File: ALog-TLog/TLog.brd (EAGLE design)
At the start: 124.1 x 45.3 mm, 101 parts, among them IC1 ATMEGA644M, J6 5.5x2.1mm Barrel, Q5 MOSFET_PCH-IRLML2244, Q6 MOSFET_PCH-IRLML2244, Q7 MOSFET_PCH-IRLML2244, Q8 MOSFET-NCH-BSS138, Q9 MOSFET-NCH-BSS138, U2 FT231X-Q, U3 915MHz, U4 SX1509, X2 87832-14

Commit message: Presumptive Final gerbers for TLog Mrk 1.1
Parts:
- ISP2: device adafruit:AVRISP -> bschulz:AVRISP
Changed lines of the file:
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@@
 <?xml version="1.0" encoding="utf-8"?>
 <!DOCTYPE eagle SYSTEM "eagle.dtd">
-<eagle version="8.3.2">
+<eagle version="8.5.1">
 <drawing>
 <settings>
@@
 <layer number="22" name="bPlace" color="7" fill="1" visible="yes" active="yes"/>
 <layer number="23" name="tOrigins" color="15" fill="1" visible="yes" active="yes"/>
-<layer number="24" name="bOrigins" color="15" fill="1" visible="yes" active="yes"/>
-<layer number="25" name="tNames" color="7" fill="1" visible="yes" active="yes"/>
-<layer number="26" name="bNames" color="7" fill="1" visible="yes" active="yes"/>
-<layer number="27" name="tValues" color="7" fill="1" visible="yes" active="yes"/>
-<layer number="28" name="bValues" color="7" fill="1" visible="yes" active="yes"/>
+<layer number="24" name="bOrigins" color="15" fill="1" visible="no" active="yes"/>
+<layer number="25" name="tNames" color="7" fill="1" visible="no" active="yes"/>
+<layer number="26" name="bNames" color="7" fill="1" visible="no" active="yes"/>
+<layer number="27" name="tValues" color="7" fill="1" visible="no" active="yes"/>
+<layer number="28" name="bValues" color="7" fill="1" visible="no" active="yes"/>
 <layer number="29" name="tStop" color="7" fill="3" visible="no" active="yes"/>
 <layer number="30" name="bStop" color="7" fill="6" visible="no" active="yes"/>
@@
 <layer number="37" name="tTest" color="7" fill="1" visible="no" active="yes"/>
 <layer number="38" name="bTest" color="7" fill="1" visible="no" active="yes"/>
-<layer number="39" name="tKeepout" color="4" fill="11" visible="yes" active="yes"/>
-<layer number="40" name="bKeepout" color="1" fill="11" visible="yes" active="yes"/>
-<layer number="41" name="tRestrict" color="4" fill="10" visible="yes" active="yes"/>
-<layer number="42" name="bRestrict" color="1" fill="10" visible="yes" active="yes"/>
+<layer number="39" name="tKeepout" color="4" fill="11" visible="no" active="yes"/>
+<layer number="40" name="bKeepout" color="1" fill="11" visible="no" active="yes"/>
+<layer number="41" name="tRestrict" color="4" fill="10" visible="no" active="yes"/>
+<layer number="42" name="bRestrict" color="1" fill="10" visible="no" active="yes"/>
 <layer number="43" name="vRestrict" color="2" fill="10" visible="no" active="yes"/>
 <layer number="44" name="Drills" color="7" fill="1" visible="yes" active="yes"/>
@@
 <wire x1="0.127" y1="45.36525" x2="0.127" y2="0.09525" width="0.254" layer="20"/>
 <rectangle x1="28.477" y1="25.804" x2="28.757" y2="26.254" layer="29"/>
-<text x="4.699" y="39.497" size="1.778" layer="51" font="vector" ratio="10" rot="SR180">RST</text>
-<text x="4.953" y="7.493" size="1.778" layer="51" font="vector" ratio="10" rot="SR180">LOG</text>
+<text x="5.08" y="39.497" size="1.778" layer="51" font="vector" ratio="10" rot="SR180">RST</text>
+<text x="5.08" y="7.747" size="1.778" layer="51" font="vector" ratio="10" rot="SR180">LOG</text>
 <text x="15.60625625" y="8.755959375" size="1.27" layer="51" font="vector" ratio="10" rot="SR180">GND</text>
 <text x="18.377803125" y="9.614803125" size="1.27" layer="51" font="vector" ratio="10" rot="SR225">A0</text>
@@
 parntnership with
 Northern Widget LLC</text>
-<text x="44.7664" y="11.284" size="0.6096" layer="22" rot="MR0">TM</text>
+<text x="43.736" y="10.994" size="0.8128" layer="22" font="vector" ratio="20" rot="MR0" align="bottom-right">TM</text>
 </plain>
 <attributes>
@@
 <param name="dpMaxLengthDifference" value="10mm"/>
 <param name="dpGapFactor" value="2.5"/>
-<param name="checkGrid" value="0"/>
 <param name="checkAngle" value="0"/>
 <param name="checkFont" value="1"/>
 <param name="checkRestrict" value="1"/>
+<param name="checkStop" value="0"/>
+<param name="checkValues" value="0"/>
 <param name="useDiameter" value="13"/>
 <param name="maxErrors" value="50"/>
@@
 <attribute name="MPN" value="MF-NSMF020-2" x="79.8195" y="22.352" size="1.778" layer="27" rot="R180" display="off"/>
 </element>
-<element name="ISP2" library="adafruit" library_urn="urn:adsk.eagle:library:420" package="AVRISP" value="AVRISP-6" x="21.209" y="37.084" smashed="yes" rot="R90">
+<element name="ISP2" library="bschulz" package="AVRISP" value="AVRISP-6" x="21.209" y="37.084" smashed="yes" rot="R90">
 <attribute name="DIGIKEY" value="609-3234-ND" x="21.209" y="37.084" size="1.778" layer="27" rot="R90" display="off"/>
 <attribute name="MF" value="Amphenol" x="21.209" y="37.084" size="1.778" layer="27" rot="R90" display="off"/>

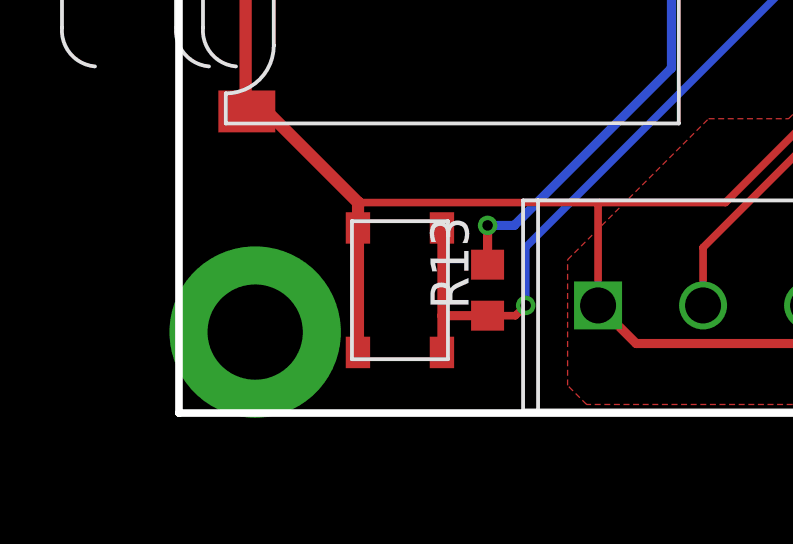
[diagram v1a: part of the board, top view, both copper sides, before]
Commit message: Final Gerbers for TLog Mrk 1.1
Gerbers_9.zip contains the gerber files used in the TLog 1.1 production run (order placed on 1/5/2017)
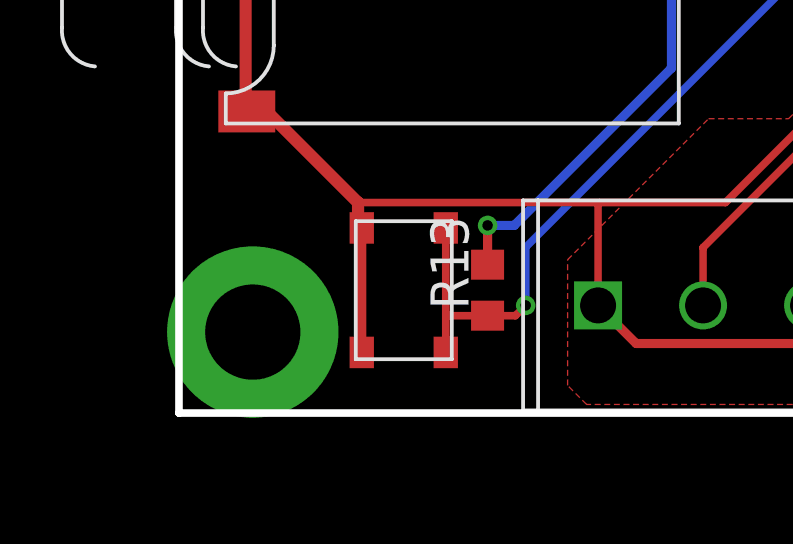
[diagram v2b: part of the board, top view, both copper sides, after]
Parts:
- moved U$5 0.13 mm to (7.62, 4.19)
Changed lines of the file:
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@@
 <?xml version="1.0" encoding="utf-8"?>
 <!DOCTYPE eagle SYSTEM "eagle.dtd">
-<eagle version="8.5.1">
+<eagle version="8.3.0">
 <drawing>
 <settings>
@@
 <setting verticaltext="up"/>
 </settings>
-<grid distance="0.127" unitdist="mm" unit="mil" style="lines" multiple="1" display="no" altdistance="0.0635" altunitdist="mm" altunit="mil"/>
+<grid distance="0.127" unitdist="mm" unit="mm" style="lines" multiple="1" display="no" altdistance="0.0635" altunitdist="mm" altunit="mm"/>
 <layers>
 <layer number="1" name="Top" color="4" fill="1" visible="yes" active="yes"/>
@@
 <layer number="22" name="bPlace" color="7" fill="1" visible="yes" active="yes"/>
 <layer number="23" name="tOrigins" color="15" fill="1" visible="yes" active="yes"/>
-<layer number="24" name="bOrigins" color="15" fill="1" visible="no" active="yes"/>
-<layer number="25" name="tNames" color="7" fill="1" visible="no" active="yes"/>
-<layer number="26" name="bNames" color="7" fill="1" visible="no" active="yes"/>
-<layer number="27" name="tValues" color="7" fill="1" visible="no" active="yes"/>
-<layer number="28" name="bValues" color="7" fill="1" visible="no" active="yes"/>
+<layer number="24" name="bOrigins" color="15" fill="1" visible="yes" active="yes"/>
+<layer number="25" name="tNames" color="7" fill="1" visible="yes" active="yes"/>
+<layer number="26" name="bNames" color="7" fill="1" visible="yes" active="yes"/>
+<layer number="27" name="tValues" color="7" fill="1" visible="yes" active="yes"/>
+<layer number="28" name="bValues" color="7" fill="1" visible="yes" active="yes"/>
 <layer number="29" name="tStop" color="7" fill="3" visible="no" active="yes"/>
 <layer number="30" name="bStop" color="7" fill="6" visible="no" active="yes"/>
@@
 <layer number="37" name="tTest" color="7" fill="1" visible="no" active="yes"/>
 <layer number="38" name="bTest" color="7" fill="1" visible="no" active="yes"/>
-<layer number="39" name="tKeepout" color="4" fill="11" visible="no" active="yes"/>
-<layer number="40" name="bKeepout" color="1" fill="11" visible="no" active="yes"/>
-<layer number="41" name="tRestrict" color="4" fill="10" visible="no" active="yes"/>
-<layer number="42" name="bRestrict" color="1" fill="10" visible="no" active="yes"/>
+<layer number="39" name="tKeepout" color="4" fill="11" visible="yes" active="yes"/>
+<layer number="40" name="bKeepout" color="1" fill="11" visible="yes" active="yes"/>
+<layer number="41" name="tRestrict" color="4" fill="10" visible="yes" active="yes"/>
+<layer number="42" name="bRestrict" color="1" fill="10" visible="yes" active="yes"/>
 <layer number="43" name="vRestrict" color="2" fill="10" visible="no" active="yes"/>
 <layer number="44" name="Drills" color="7" fill="1" visible="yes" active="yes"/>
@@
 <text x="54.527903125" y="9.6892" size="1.27" layer="51" font="vector" ratio="10" rot="SR225">A5</text>
 <text x="58.382803125" y="10.72060625" size="1.27" layer="51" font="vector" ratio="10" rot="SR225">INT1</text>
-<text x="62.252453125" y="9.8245625" size="1.27" layer="51" font="vector" ratio="10" rot="SR225">5V</text>
+<text x="61.490453125" y="10.2055625" size="1.27" layer="51" font="vector" ratio="10" rot="SR225">5V</text>
 <text x="65.621803125" y="10.29470625" size="1.27" layer="51" font="vector" ratio="10" rot="SR225">3V3</text>
 <text x="69.080296875" y="10.376803125" size="1.27" layer="51" font="vector" ratio="10" rot="SR225">GND</text>
@@
 <text x="21.87575" y="33.49625" size="1.27" layer="51" font="vector" ratio="10" rot="SR180">ISP</text>
 <text x="115.22075" y="44.7675" size="1.27" layer="51" font="vector" ratio="10" rot="SR180">VIN</text>
-<text x="32.639" y="44.831" size="1.27" layer="51" font="vector" ratio="10" rot="SR180">A6</text>
-<text x="36.576" y="44.831" size="1.27" layer="51" font="vector" ratio="10" rot="SR180">A7</text>
-<text x="39.878" y="44.831" size="1.27" layer="51" font="vector" ratio="10" rot="SR180">A8</text>
-<text x="43.40225" y="44.831" size="1.27" layer="51" font="vector" ratio="10" rot="SR180">A9</text>
-<text x="47.625" y="44.831" size="1.27" layer="51" font="vector" ratio="10" rot="SR180">A10</text>
+<text x="32.512" y="44.831" size="1.27" layer="51" font="vector" ratio="10" rot="SR180">A6</text>
+<text x="35.814" y="44.831" size="1.27" layer="51" font="vector" ratio="10" rot="SR180">A7</text>
+<text x="39.243" y="44.831" size="1.27" layer="51" font="vector" ratio="10" rot="SR180">A8</text>
+<text x="42.76725" y="44.831" size="1.27" layer="51" font="vector" ratio="10" rot="SR180">A9</text>
+<text x="47.244" y="44.831" size="1.27" layer="51" font="vector" ratio="10" rot="SR180">A10</text>
 <text x="51.562" y="44.831" size="1.27" layer="51" font="vector" ratio="10" rot="SR180">A11</text>
 <text x="54.61" y="44.831" size="1.27" layer="51" font="vector" ratio="10" rot="SR180">D0</text>
@@
 <param name="dpMaxLengthDifference" value="10mm"/>
 <param name="dpGapFactor" value="2.5"/>
+<param name="checkGrid" value="0"/>
 <param name="checkAngle" value="0"/>
 <param name="checkFont" value="1"/>
 <param name="checkRestrict" value="1"/>
-<param name="checkStop" value="0"/>
-<param name="checkValues" value="0"/>
 <param name="useDiameter" value="13"/>
 <param name="maxErrors" value="50"/>
@@
 <attribute name="VALUE_PART" value="330" x="48.641" y="33.02" size="1.778" layer="27" rot="R180" display="off"/>
 </element>
-<element name="U$5" library="bschulz" package="SWITCH_4.2X3.2" value="BUTTON4.2X3.2" x="7.493" y="4.191" smashed="yes" rot="R90"/>
+<element name="U$5" library="bschulz" package="SWITCH_4.2X3.2" value="BUTTON4.2X3.2" x="7.62" y="4.191" smashed="yes" rot="R90"/>
 <element name="R13" library="bschulz" package="R0603" value="10k" x="10.414" y="4.191" smashed="yes" rot="R90">
 <attribute name="DIGIKEY" value="311-10.0KHRCT-ND" x="10.414" y="4.191" size="1.778" layer="27" rot="R90" display="off"/>
@@
 <contactref element="U$5" pad="2"/>
 <wire x1="13.1445" y1="43.59275" x2="12.99125" y2="43.746" width="0.4064" layer="1"/>
-<wire x1="6.093" y1="6.090375" x2="6.093" y2="6.266" width="0.4064" layer="1"/>
-<wire x1="6.093" y1="6.090375" x2="6.093" y2="2.116" width="0.4064" layer="1"/>
+<wire x1="6.093" y1="6.090375" x2="6.22" y2="6.266" width="0.4064" layer="1"/>
 <wire x1="9.035" y1="43.746" x2="9.02" y2="43.731" width="0.4064" layer="1"/>
 <wire x1="12.99125" y1="43.746" x2="9.035" y2="43.746" width="0.4064" layer="1"/>
@@
 <wire x1="71.374" y1="9.525" x2="71.374" y2="10.834" width="0.3048" layer="1"/>
 <wire x1="75.3745" y1="9.525" x2="71.374" y2="9.525" width="0.3048" layer="1"/>
+<wire x1="6.22" y1="6.266" x2="6.22" y2="2.116" width="0.3048" layer="1"/>
+<wire x1="101.292" y1="33.21" x2="101.692" y2="33.21" width="0" layer="19" extent="1-1"/>
+<wire x1="100.892" y1="33.21" x2="101.292" y2="33.21" width="0" layer="19" extent="1-1"/>
+<wire x1="100.492" y1="33.21" x2="100.892" y2="33.21" width="0" layer="19" extent="1-1"/>
+<wire x1="101.092" y1="32.385" x2="101.292" y2="33.21" width="0" layer="19" extent="1-1"/>
+<wire x1="101.092" y1="31.75" x2="101.092" y2="32.35" width="0" layer="19" extent="1-1"/>
+<wire x1="101.092" y1="31.15" x2="101.092" y2="31.75" width="0" layer="19" extent="1-1"/>
+<wire x1="96.818975" y1="35.184975" x2="96.774" y2="35.7806" width="0" layer="19" extent="1-1"/>
+<wire x1="95.367" y1="22.094" x2="94.5642" y2="22.9108" width="0" layer="19" extent="1-16"/>
 <wire x1="121.6025" y1="7.874" x2="121.6025" y2="7.874" width="0" layer="19" extent="1-16"/>
 <wire x1="121.6025" y1="2.794" x2="121.6025" y2="2.794" width="0" layer="19" extent="1-16"/>
+<wire x1="101.561" y1="34.798" x2="102.46329375" y2="35.7806" width="0" layer="19" extent="1-1"/>
+<wire x1="30.861" y1="35.336" x2="32.4162" y2="34.5274" width="0" layer="19" extent="1-1"/>
+<wire x1="106.299" y1="32.446" x2="104.394" y2="32.446" width="0" layer="19" extent="1-1"/>
+<wire x1="86.94345" y1="25.4635" x2="87.767" y2="22.094" width="0" layer="19" extent="1-1"/>
 </signal>
 <signal name="RST">
@@
 </signal>
 <signal name="N$12">
-<via x="2.667" y="2.794" extent="1-16" drill="3.175" shape="octagon"/>
+<via x="2.587625" y="2.794" extent="1-16" drill="3.175" shape="octagon"/>
 </signal>
 <signal name="N$17">
@@
 <contactref element="U$5" pad="3"/>
 <contactref element="R13" pad="1"/>
-<wire x1="8.893" y1="3.341" x2="8.893" y2="6.266" width="0.3048" layer="1"/>
-<wire x1="8.893" y1="3.341" x2="8.893" y2="2.116" width="0.3048" layer="1"/>
-<wire x1="8.893" y1="3.341" x2="10.414" y2="3.341" width="0.3048" layer="1"/>
-<wire x1="10.414" y1="3.341" x2="11.342" y2="3.341" width="0.254" layer="1"/>
+<wire x1="11.342" y1="3.341" x2="10.414" y2="3.341" width="0.254" layer="1"/>
 <wire x1="11.342" y1="3.341" x2="11.684" y2="3.683" width="0.254" layer="1"/>
 <via x="11.684" y="3.683" extent="1-16" drill="0.35" shape="octagon"/>
@@
 <wire x1="54.737" y1="22.252325" x2="56.31395625" y2="22.252325" width="0.254" layer="1"/>
 <wire x1="56.31395625" y1="22.252325" x2="57.15" y2="21.41628125" width="0.254" layer="1"/>
+<wire x1="9.02" y1="3.314171875" x2="9.02" y2="6.266" width="0.254" layer="1"/>
+<wire x1="9.02" y1="3.314171875" x2="9.02" y2="2.116" width="0.254" layer="1"/>
+<wire x1="10.414" y1="3.341" x2="9.046828125" y2="3.341" width="0.254" layer="1"/>
+<wire x1="9.046828125" y1="3.341" x2="9.02" y2="3.314171875" width="0.254" layer="1"/>
 </signal>
 <signal name="3V3">

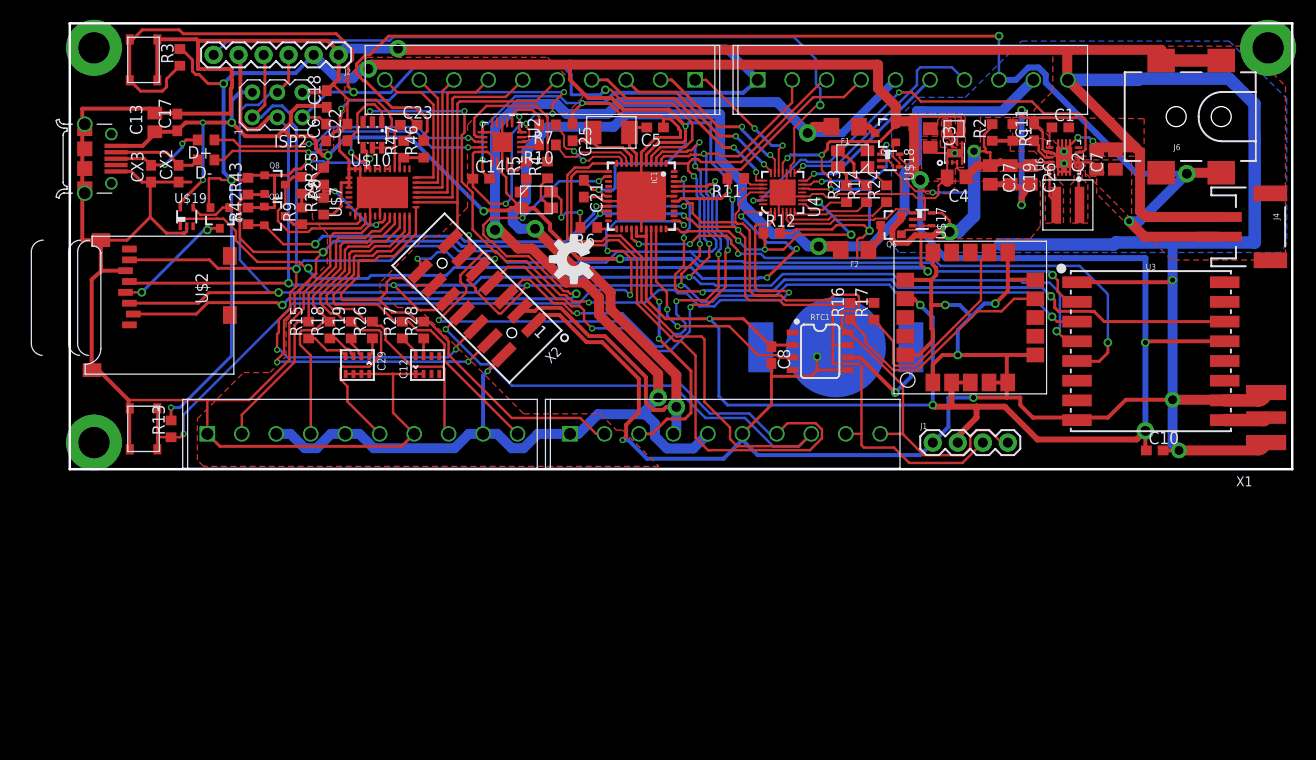
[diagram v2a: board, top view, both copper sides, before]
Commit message: Issue Fix
Patial fix of issues: #12, #9, #8 (fixed in schematic, but not fully routed)
Full fix of issues: #10, #7
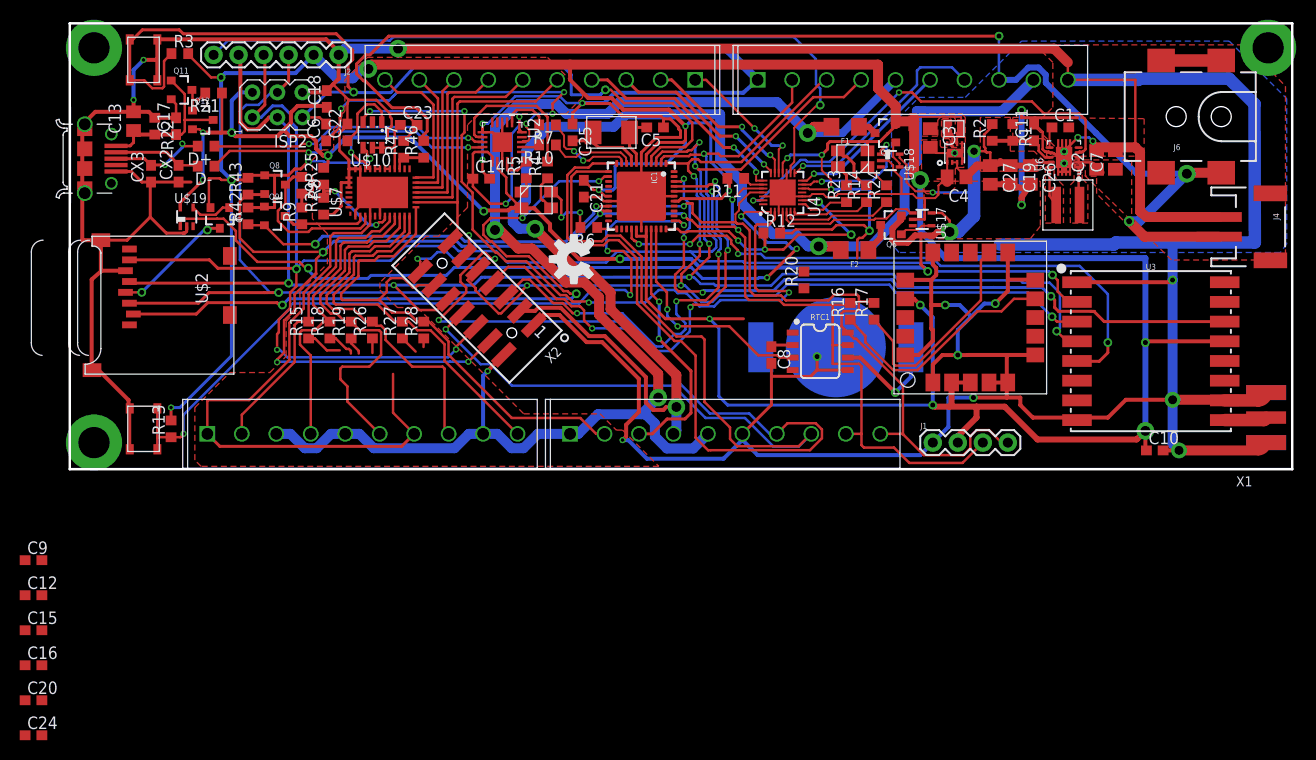
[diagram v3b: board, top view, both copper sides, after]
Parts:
- removed C29: 10nF, rc-master-smd:CECJ-1206
- added C15, C16, C20, C24, C9: (no value), bschulz_passives:C0603
- added Q11: MOSFET-NCH-BSS138, bschulz:SOT23-3
- added Q12: MOSFET_PCH-IRLML2244, bschulz:SOT23-3
- added R20: 180k, bschulz_passives:R0603
- added R21, R22: 10k, rcl:R0603
- C12: value 10nF -> (none); device rc-master-smd:CECJ-1206 -> bschulz_passives:C0603
- moved C12 46.3 mm to (-3.56, -12.7)
- moved C13 2.16 mm to (6.60, 35.4)
- moved D+ 0.63 mm to (14.0, 32.9)
- moved D- 0.63 mm to (14.0, 30.9)
- moved C17 0.40 mm to (10.9, 34.9)
- moved R3 0.38 mm to (11.3, 42.3), turned to 0 degrees
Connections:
- removed net N$17: C12.B2, R28.1
- removed net N$19: C29.B1, R19.1
- removed net N$24: C29.A1, R26.1
- removed net N$44: C29.D1, R15.1
- removed net N$45: C29.C1, R18.1
- removed net N$48: C12.A2, R27.1
- new net 5V_EXT: R25.2
- new net N$34: Q11.3, Q12.1, R21.2
- new net VUSB: C13.1, C17.1, MICRO_USB.1, Q11.1, Q12.3, R22.2
- net 3V3: now also R20.2; no longer C8.1, RTC1.2
- net 5V: now also Q12.2, R21.1; no longer C13.1, C17.1, MICRO_USB.1, R25.2
- net ADC0: now also C9.1
- net ADC1: now also C12.1
- net ADC2: now also C15.1
- net ADC3: now also C16.1
- net ADC4: now also C20.1
- net ADC5: now also C24.1
- net EXT_3.3V: now also C8.1, RTC1.2
- net GND: now also C12.2, C15.2, C16.2, C20.2, C24.2, C9.2, Q11.2, R15.1, R18.1, R19.1, R22.1, R26.1, R27.1, R28.1; no longer C12.A1, C12.B1, C29.A2, C29.B2, C29.C2, C29.D2
- net REF_CTRL: now also R20.1
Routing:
- net GND: track 841.5 -> 822.7 mm, vias 18 -> 20
- net VUSB: track 0.00 -> 17.7 mm
- net 3V3: track 426.5 -> 418.8 mm
- net 5V: track 185.7 -> 178.4 mm
- net N$44: track 4.50 -> 0.00 mm
- net N$34: track 0.00 -> 3.70 mm
- net N$45: track 3.30 -> 0.00 mm
- net N$48: track 2.36 -> 0.00 mm
- net N$19: track 2.23 -> 0.00 mm
- net EXT_3.3V: track 147.6 -> 149.8 mm
- net N$24: track 1.94 -> 0.00 mm
- net N$17: track 1.81 -> 0.00 mm
- net N$38: track 29.2 -> 28.7 mm
